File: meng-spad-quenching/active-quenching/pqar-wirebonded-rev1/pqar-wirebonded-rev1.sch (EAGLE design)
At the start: 47 parts, among them IC1 NL17SZ125, IC14 LTC1711, IC17 NL17SZ125, IC2 LTC1711, IC20 NC7WZ16P6X, IC24 TLV272DGK, IC3 NC7SV74K8X, T1 MMBTH10−4LT1G, U1 SN74LVC1G123DCUT, X1 V_A, X2 OUT, X3 V_LOGIC, X4 I_HOLDOFF

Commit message: got everything to initially fit on the board
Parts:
- removed C70: CAP CER 100PF 50V C0G 0603 5%, rcl-modified-footprints:C-EUC0603
- removed C77, C80, C93: CAP CER 0.1UF 10V X7R 0402 10%, rcl-modified-footprints:C-EUC0402
- removed C78: CAP CER 10000PF 10V X7R 0402 10%, rcl-modified-footprints:C-EUC0402
- removed C81: CAP CER 10000PF 10V X7R 0402 10%, rcl:C-EUC0402
- removed IC14: LTC1711, meng:LTC1711
- removed IC17: NL17SZ125, 74xx-little-de:74AHC1G125DCK
- removed IC24: TLV272DGK, meng:TLV272DGK
- removed R53, R61: RES SMD 220K OHM 1% 1/10W 0603, rcl-modified-footprints:R-EU_R0603
- removed R54: RES SMD 10K OHM 1% 1/10W 0603, rcl-modified-footprints:R-EU_R0603
- removed T1: MMBTH10−4LT1G, transistor:MMBTH10LT1-NPN-SOT23-BEC
- removed TP2: AV_DET, testpad:TPTP10R
- added C10, C11, C9: IPDiA 935131425610, rcl-modified-footprints:C-EUC0603
- added C12: CAP CER 0.1UF 50V X7R 0805 5%, rcl-modified-footprints:C-EUC0805
- added C13, C14, C8: DNP, rcl-modified-footprints:C-EUC0603
- added C15: CAP CER 0.1UF 50V X7R 0603 5%, rcl-modified-footprints:C-EUC0603
- added IC4: BCV62, meng:BCV62
- added IC5: 74AHC1G14DCK, 74xx-little-us:74AHC1G14DCK
- added IC6: SPAD-GENERIC, meng:SPAD-GENERIC
- added IC8: 74LVC1G02DCK, 74xx-little-us:74LVC1G02DCK
- added L1, L2, L3: Samsung CIM05J152NC, meng:INDUCTOR0402
- added R12, R13: RES SMD 0R 0603, rcl-modified-footprints:R-EU_R0603
- added TP1, TP3: AV_DET, testpad:TPTP10R
- C2: value CAP CER 100PF 50V C0G 0603 5% -> CAP CER 0.1UF 50V X7R 0603 5%
- R11: value DNP -> RES SMD 0R 0603
- R7: value Vishay FC0603E50R0BTBST1 -> DNP
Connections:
- removed net CAP_!RESET: IC17A.OE
- removed net N$1: C7.1, IC2.+IN, R5.2, R6.1
- removed net N$11: IC14.-IN
- removed net N$12: IC20.IN1, IC20.IN2, R11.2, U1.Q
- removed net N$15: IC14.V-
- removed net N$3: C2.1, R2.1, X1C.1
- removed net N$4: C1.2, IC2.-IN, R3.2, R4.1
- removed net N$6: IC3.CLK, R8.2, R9.2
- removed net NC_RESET: IC3.Q
- removed net ONE_SHOT_CAP: C70.1, IC14.+IN, IC17A.O, T1.C
- removed net ONE_SHOT_FB: R53.1, R54.1, T1.E
- removed net ONE_SHOT_VGND: IC24_A.-IN, R53.2, R61.1
- removed net PP_N5V0_ANALOG: C80.1, IC24_A.V-, R54.2
- removed net PP_P5V0_ANALOG: C77.1, C78.1, C93.1, IC14.V+, IC24_A.V+
- removed net VREF_ONE_SHOT_CCS: R61.2
- new net !EN_DRIVER: IC1A.OE, IC8A.O
- new net !QUENCH: IC5A.O, R11.2
- new net AV_DET_REF: C13.1, C7.1, IC2.+IN, R5.2, R6.1
- new net CLK_RESET: IC3.CLK, R11.1, R8.2, R9.2
- new net DRIVER_IN: IC1A.I, IC8A.I0, R13.1, R7.1
- new net KATHODE_C: C1.2, C14.1, IC2.-IN, R3.2, R4.1
- new net N$7: C8.1, IC3.!CLR, R12.2
- new net N$8: L2.P$1, X4C.1
- new net QUENCH: IC20.IN1, IC20.IN2, IC5A.I, R13.2, U1.Q
- new net RESET: IC3.Q, IC8A.I1
- new net V_A: L3.P$1, X1C.1
- new net V_A_FILT: C12.1, C2.1, L3.P$2, R2.1
- net !AV_DET: now also C14.2, TP3.TP
- net !RESET: now also R12.1; no longer IC1A.OE, IC3.!CLR
- net +5V: now also C10.1, C11.1, C9.1, IC1P.VCC, IC4.E_IN, IC4.E_OUT, IC5P.VCC, IC8P.VCC, L1.P$2; no longer C81.1, IC17A.I, X3C.1
- net ANODE: now also IC6.SPAD_ANODE
- net AV_DET: now also C13.2, TP1.TP; no longer TP2.TP
- net GND: now also C10.2, C11.2, C12.2, C15.2, C8.2, C9.2, IC1P.GND, IC5P.GND, IC6.GND, IC8P.GND, R7.2; no longer C70.2, C77.2, C78.2, C80.2, C81.2, C93.2, IC14.GND, IC14.LEN, IC1A.I, IC24_A.+IN
- net KATHODE: now also IC6.SPAD_CATHODE
- net N$17: now also IC4.C_OUT
- net N$2: now also C15.1, IC4.BC_IN, L2.P$2; no longer X4C.1
- net N$5: now also L1.P$1, X3C.1; no longer IC24_A.OUT, T1.B
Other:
- note added: "CAP SILICON 0.1UF 11V 0603"
- note added: "FERRITE BEAD 0402"
- note removed: "5V"
- note removed: "Film cap."
- note removed: "ONE_SHOT_CAP"
- note removed: "This CCS BJT is always in FAR"
- note removed: "avalanche detected"
- note removed: "comp triggered"
- note removed: "holdoff time"
- moved on the sheet: C1, C2, C3, C4, C5, C6, C7, C83, H1, H2, H3, H4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

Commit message: More routing, add or gate for forcing quenching
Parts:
- added C16: IPDiA 935131425610, rcl-modified-footprints:C-EUC0603
- added IC7: 74AUC1G32DCK, 74xx-little-us:74AUC1G32DCK
- added L4: Samsung CIM05J152NC, meng:INDUCTOR0402
- added R14, R15, R16: DNP, rcl-modified-footprints:R-EU_R0603
- added X5: FORCE_QUENCH, meng:MMCXBIGPAD
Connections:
- net N$17 renamed HOLDOFF_CAP
- net N$2 renamed I_HOLDOFF_FILT
- net N$29 renamed OUT
- net N$7 renamed !RESET_RC
- net N$8 renamed I_HOLDOFF
- net PHOTON_COUNT_OUT renamed OUT_R
- new net FORCE_QUENCH: IC7A.I1, R15.1, X5C.1
- new net HOLDOFF_TIMER: IC20.IN1, IC20.IN2, IC7A.I0, R16.2, U1.Q
- new net VDD_COMP: C3.1, IC2.V+, L4.P$2, R3.1, R5.1
- net +5V: now also C16.1, IC7P.VCC, L4.P$1; no longer C3.1, IC2.V+, R3.1, R5.1
- net CLK_RESET: now also R14.1
- net GND: now also C16.2, IC7P.GND, R15.2, X5C.GND, X5G.GND@1, X5G.GND@2, X5G.GND@3
- net QUENCH: now also IC7A.O, R14.2, R16.1; no longer IC20.IN1, IC20.IN2, U1.Q
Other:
- note added: "Active quenching"
- note added: "Bypass for debugging"
- note added: "Optional AC-coupled hysteresis"
- note added: "Passive quenching"
- note removed: "Avalanche Detector Todo: add AC-coupled hysteresis (see UAD) add ferrite bead to supply"
- moved on the sheet: C15, C83, IC20, IC4, IC5, L2, R11, R12

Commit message: first pass routing done, DRC not clean
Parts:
- removed C83: CAP CER 0.1UF 10V X7R 0402 10%, rcl:C-EUC0402
- added C17: CAP CER 0.1UF 50V X7R 0805 5%, rcl-modified-footprints:C-EUC0805
- added C18: CAP CER 0.1UF 50V X7R 0603 5%, rcl-modified-footprints:C-EUC0603
- added L5: Samsung CIM05J152NC, meng:INDUCTOR0402
- added R17: RES SMD 0R 0805, rcl-modified-footprints:R-EU_R0805
- C13, C14, C8: device rcl-modified-footprints:C-EUC0603 -> rcl-modified-footprints:C-EUC0805
- C2: value CAP CER 0.1UF 50V X7R 0603 5% -> CAP CER 0.1UF 50V X7R 0805 5%; device rcl-modified-footprints:C-EUC0603 -> rcl-modified-footprints:C-EUC0805
- C5: value CAP CER 0.1UF 50V X7R 0805 10% -> CAP CER 0.1UF 50V X7R 0805 5%; device rcl:C-EUC0603 -> rcl-modified-footprints:C-EUC0805
- IC6: value SPAD-GENERIC -> SPAD
- R10, R16, R7, R8, R9: device rcl-modified-footprints:R-EU_R0603 -> rcl-modified-footprints:R-EU_R0805
- R12, R13: value RES SMD 0R 0603 -> RES SMD 0R 0805; device rcl-modified-footprints:R-EU_R0603 -> rcl-modified-footprints:R-EU_R0805
- R15: value DNP -> RES SMD 10K OHM 1% 1/10W 0603
- R2, R3, R5: value RES SMD 1K OHM 1% 1/10W 0603 -> RES SMD 1K OHM 1% 1/10W 0805; device rcl-modified-footprints:R-EU_R0603 -> rcl-modified-footprints:R-EU_R0805
- R52: value RES SMD 49.9 OHM 1% 1/10W 0603 -> RES SMD 49.9 OHM 1% 1/10W 0805; device rcl:R-EU_R0603 -> rcl:R-EU_R0805
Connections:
- net N$16 renamed CEXT
- net N$5 renamed V_LOGIC
- new net N$1: L4.P$1, L5.P$2
- new net N$2: IC20.IN1, IC20.IN2, R17.2
- net +5V: now also C18.1, L5.P$1; no longer C83.1, L4.P$1
- net CLK_RESET: now also R17.1
- net GND: now also C17.2, C18.2; no longer C83.2
- net HOLDOFF_TIMER: no longer IC20.IN1, IC20.IN2
- net V_A: now also C17.1
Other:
- note added: "Needed to jump over a signal"
- note added: "Use 2 for escaping signals underneath"
- moved on the sheet: IC20, L1, L3, R52, X2C, X2G, X5C, X5G

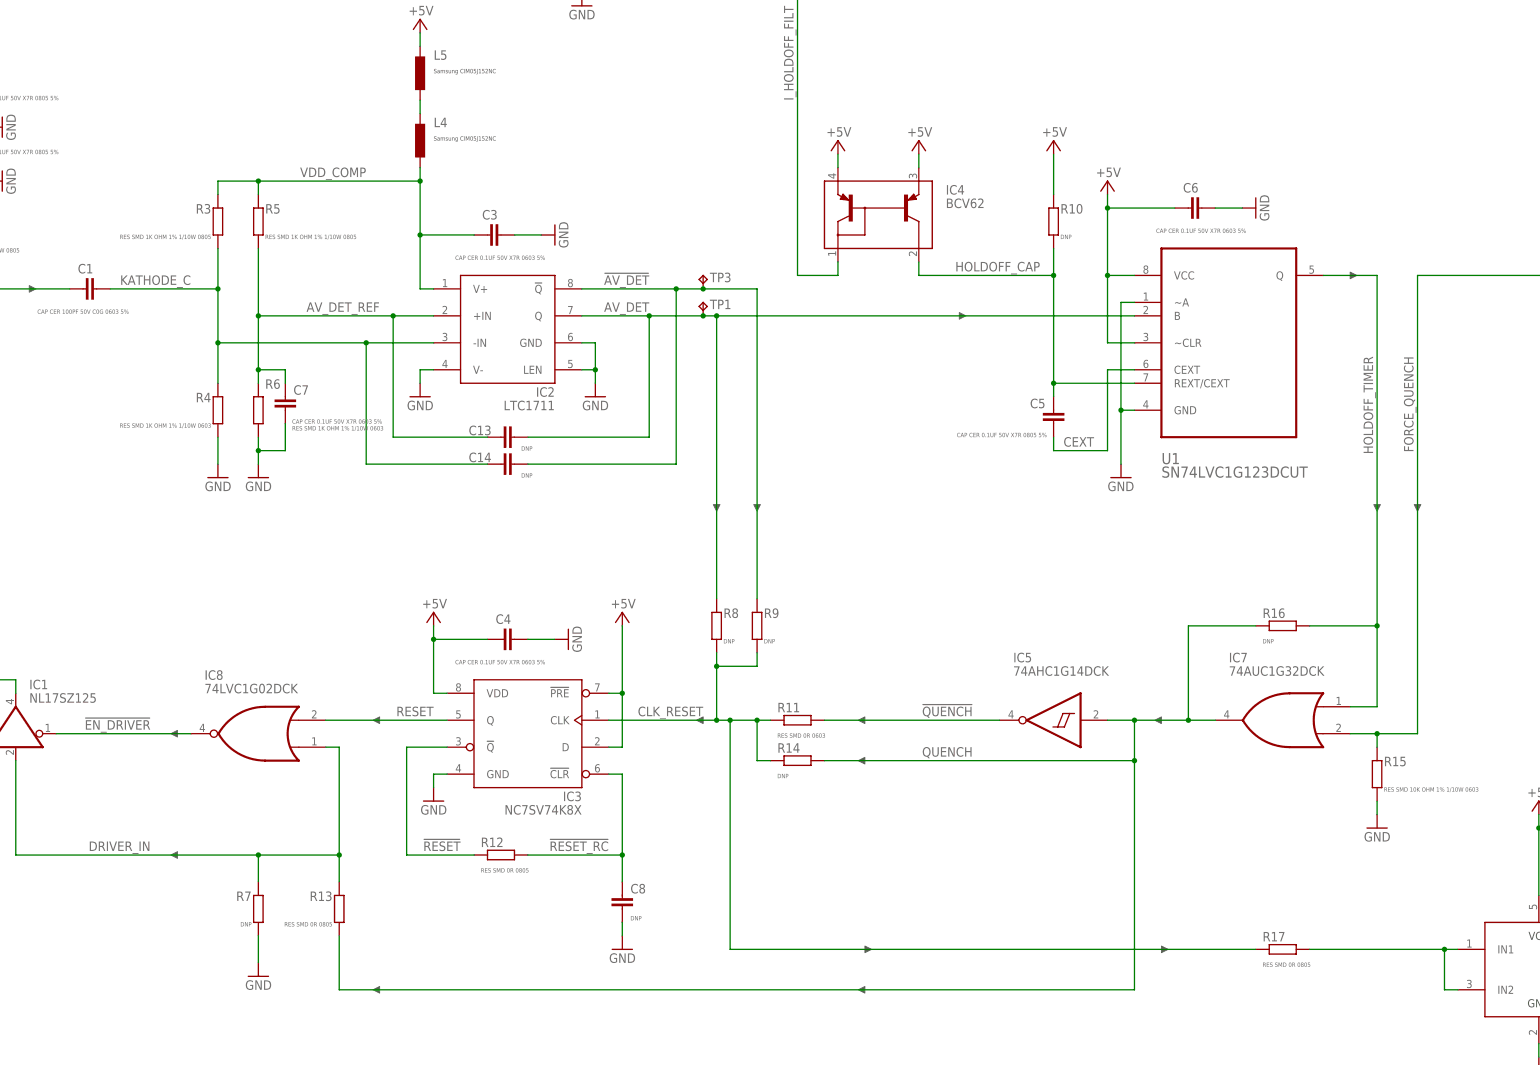
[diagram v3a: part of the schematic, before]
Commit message: Clean up routing, DRC pass
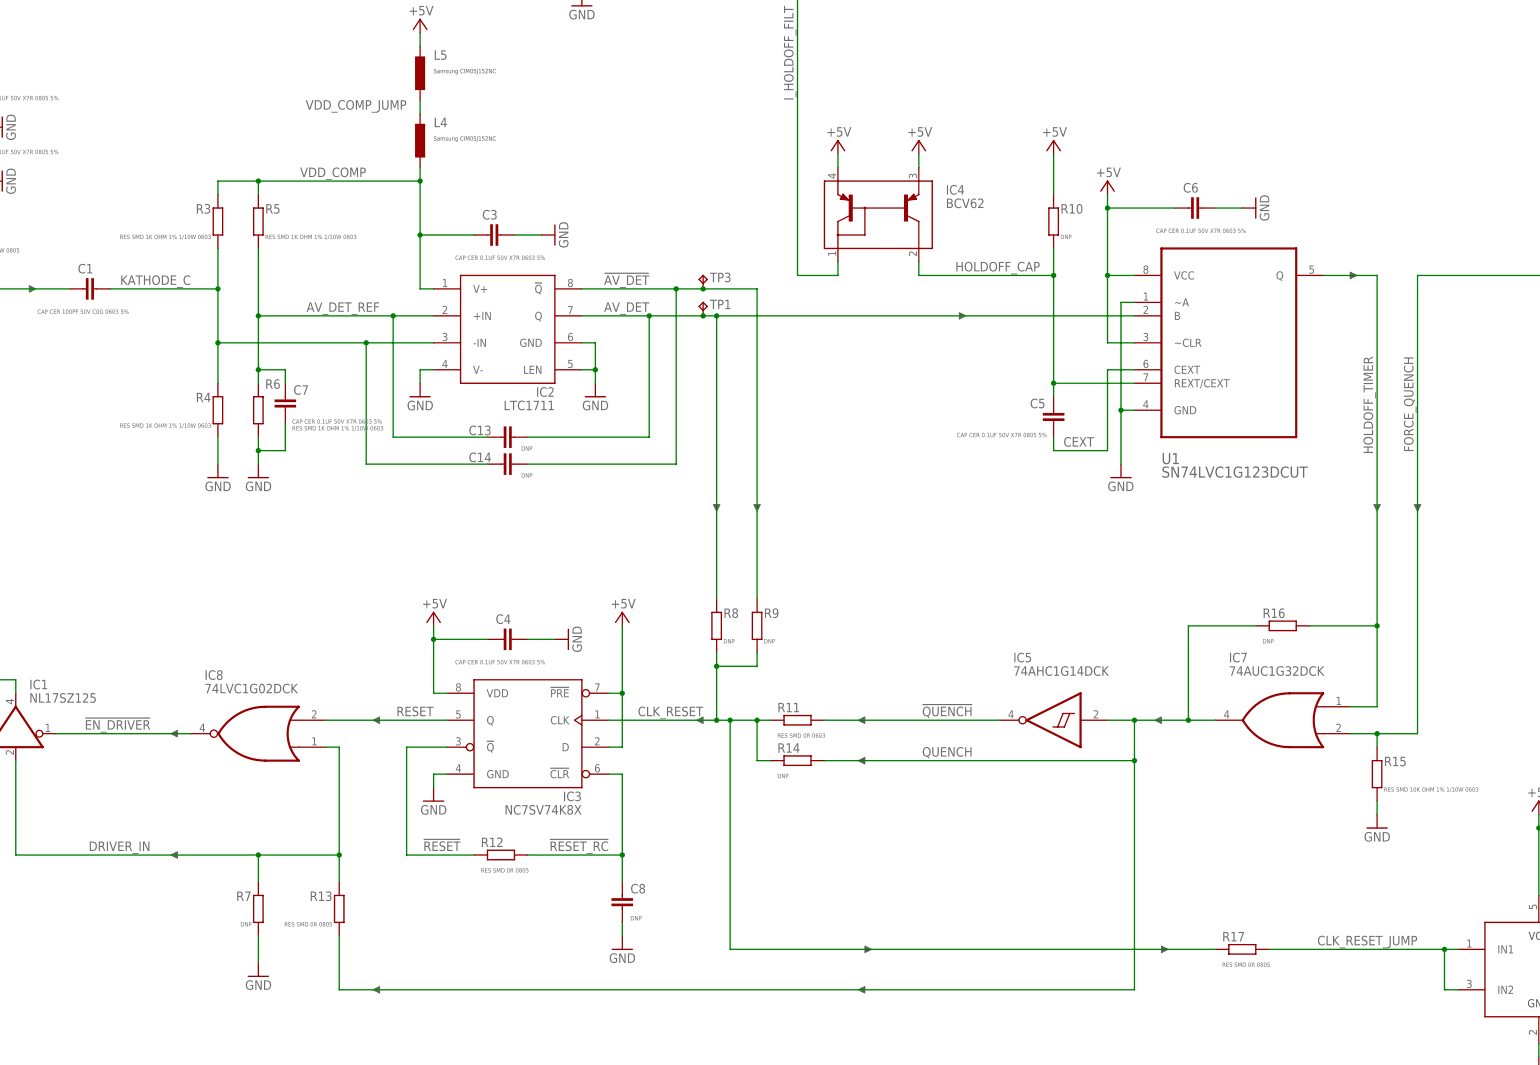
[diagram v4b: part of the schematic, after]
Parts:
- R16: device rcl-modified-footprints:R-EU_R0805 -> rcl-modified-footprints:R-EU_R0603
- R3, R5: value RES SMD 1K OHM 1% 1/10W 0805 -> RES SMD 1K OHM 1% 1/10W 0603; device rcl-modified-footprints:R-EU_R0805 -> rcl-modified-footprints:R-EU_R0603
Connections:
- net N$1 renamed VDD_COMP_JUMP
- net N$2 renamed CLK_RESET_JUMP
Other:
- moved on the sheet: R17
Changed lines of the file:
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@@
 <part name="IC3" library="meng" deviceset="NC7SV74K8X" device="" value="NC7SV74K8X"/>
 <part name="GND7" library="supply1" deviceset="GND" device=""/>
-<part name="R3" library="rcl-modified-footprints" deviceset="R-EU_" device="R0805" package3d_urn="urn:adsk.eagle:package:23553/2" value="RES SMD 1K OHM 1% 1/10W 0805"/>
+<part name="R3" library="rcl-modified-footprints" deviceset="R-EU_" device="R0603" package3d_urn="urn:adsk.eagle:package:23555/2" value="RES SMD 1K OHM 1% 1/10W 0603"/>
 <part name="R4" library="rcl-modified-footprints" deviceset="R-EU_" device="R0603" package3d_urn="urn:adsk.eagle:package:23555/2" value="RES SMD 1K OHM 1% 1/10W 0603"/>
-<part name="R5" library="rcl-modified-footprints" deviceset="R-EU_" device="R0805" package3d_urn="urn:adsk.eagle:package:23553/2" value="RES SMD 1K OHM 1% 1/10W 0805"/>
+<part name="R5" library="rcl-modified-footprints" deviceset="R-EU_" device="R0603" package3d_urn="urn:adsk.eagle:package:23555/2" value="RES SMD 1K OHM 1% 1/10W 0603"/>
 <part name="R6" library="rcl-modified-footprints" deviceset="R-EU_" device="R0603" package3d_urn="urn:adsk.eagle:package:23555/2" value="RES SMD 1K OHM 1% 1/10W 0603"/>
 <part name="GND8" library="supply1" deviceset="GND" device=""/>
@@
 <part name="X5" library="meng" deviceset="MMCX" device="BIGPAD" value="FORCE_QUENCH"/>
 <part name="GND31" library="supply1" deviceset="GND" device=""/>
-<part name="R16" library="rcl-modified-footprints" deviceset="R-EU_" device="R0805" package3d_urn="urn:adsk.eagle:package:23553/2" value="DNP"/>
+<part name="R16" library="rcl-modified-footprints" deviceset="R-EU_" device="R0603" package3d_urn="urn:adsk.eagle:package:23555/2" value="DNP"/>
 <part name="DNP19" library="meng" deviceset="ARROW_1DIR" device=""/>
 <part name="DNP20" library="meng" deviceset="ARROW_1DIR" device=""/>
@@
 <text x="287.02" y="15.24" size="1.27" layer="98">CAP SILICON 0.1UF 11V 0603</text>
 <text x="162.56" y="223.52" size="1.778" layer="98">Use 2 for escaping signals underneath</text>
-<text x="309.88" y="68.58" size="1.778" layer="98">Needed to jump over a signal</text>
+<text x="299.72" y="71.12" size="1.778" layer="98">Needed to jump over a signal</text>
 </plain>
 <instances>
@@
 <attribute name="VALUE" x="160.02" y="228.6" size="0.8128" layer="97"/>
 </instance>
-<instance part="R17" gate="G$1" x="320.04" y="63.5" smashed="yes" rot="MR180">
-<attribute name="NAME" x="316.23" y="64.9986" size="1.778" layer="95"/>
-<attribute name="VALUE" x="316.23" y="60.198" size="0.8128" layer="96"/>
+<instance part="R17" gate="G$1" x="312.42" y="63.5" smashed="yes" rot="MR180">
+<attribute name="NAME" x="308.61" y="64.9986" size="1.778" layer="95"/>
+<attribute name="VALUE" x="308.61" y="60.198" size="0.8128" layer="96"/>
 </instance>
 </instances>
@@
 <wire x1="215.9" y1="63.5" x2="215.9" y2="106.68" width="0.1524" layer="91"/>
 <junction x="215.9" y="106.68"/>
-<wire x1="314.96" y1="63.5" x2="215.9" y2="63.5" width="0.1524" layer="91"/>
+<wire x1="307.34" y1="63.5" x2="215.9" y2="63.5" width="0.1524" layer="91"/>
 <pinref part="R17" gate="G$1" pin="1"/>
 </segment>
@@
 </segment>
 </net>
-<net name="N$1" class="0">
+<net name="VDD_COMP_JUMP" class="0">
 <segment>
 <pinref part="L5" gate="G$1" pin="P$2"/>
 <pinref part="L4" gate="G$1" pin="P$1"/>
 <wire x1="157.48" y1="223.52" x2="157.48" y2="220.98" width="0.1524" layer="91"/>
-</segment>
-</net>
-<net name="N$2" class="0">
+<label x="154.94" y="223.52" size="1.778" layer="95" rot="R180"/>
+</segment>
+</net>
+<net name="CLK_RESET_JUMP" class="0">
 <segment>
 <pinref part="IC20" gate="G$1" pin="IN1"/>
@@
 <wire x1="350.52" y1="55.88" x2="350.52" y2="63.5" width="0.1524" layer="91"/>
 <junction x="350.52" y="63.5"/>
-<wire x1="350.52" y1="63.5" x2="325.12" y2="63.5" width="0.1524" layer="91"/>
+<wire x1="350.52" y1="63.5" x2="317.5" y2="63.5" width="0.1524" layer="91"/>
 <pinref part="R17" gate="G$1" pin="2"/>
-</segment>
-</net>
+<label x="345.44" y="66.04" size="1.778" layer="95" rot="R180"/>
+</segment>
+</net>
